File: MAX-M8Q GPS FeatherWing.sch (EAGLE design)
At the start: 28 parts, among them Q1 DMG3415U-7, Q2 2N2222, SW1 KMR2, X1 uFL

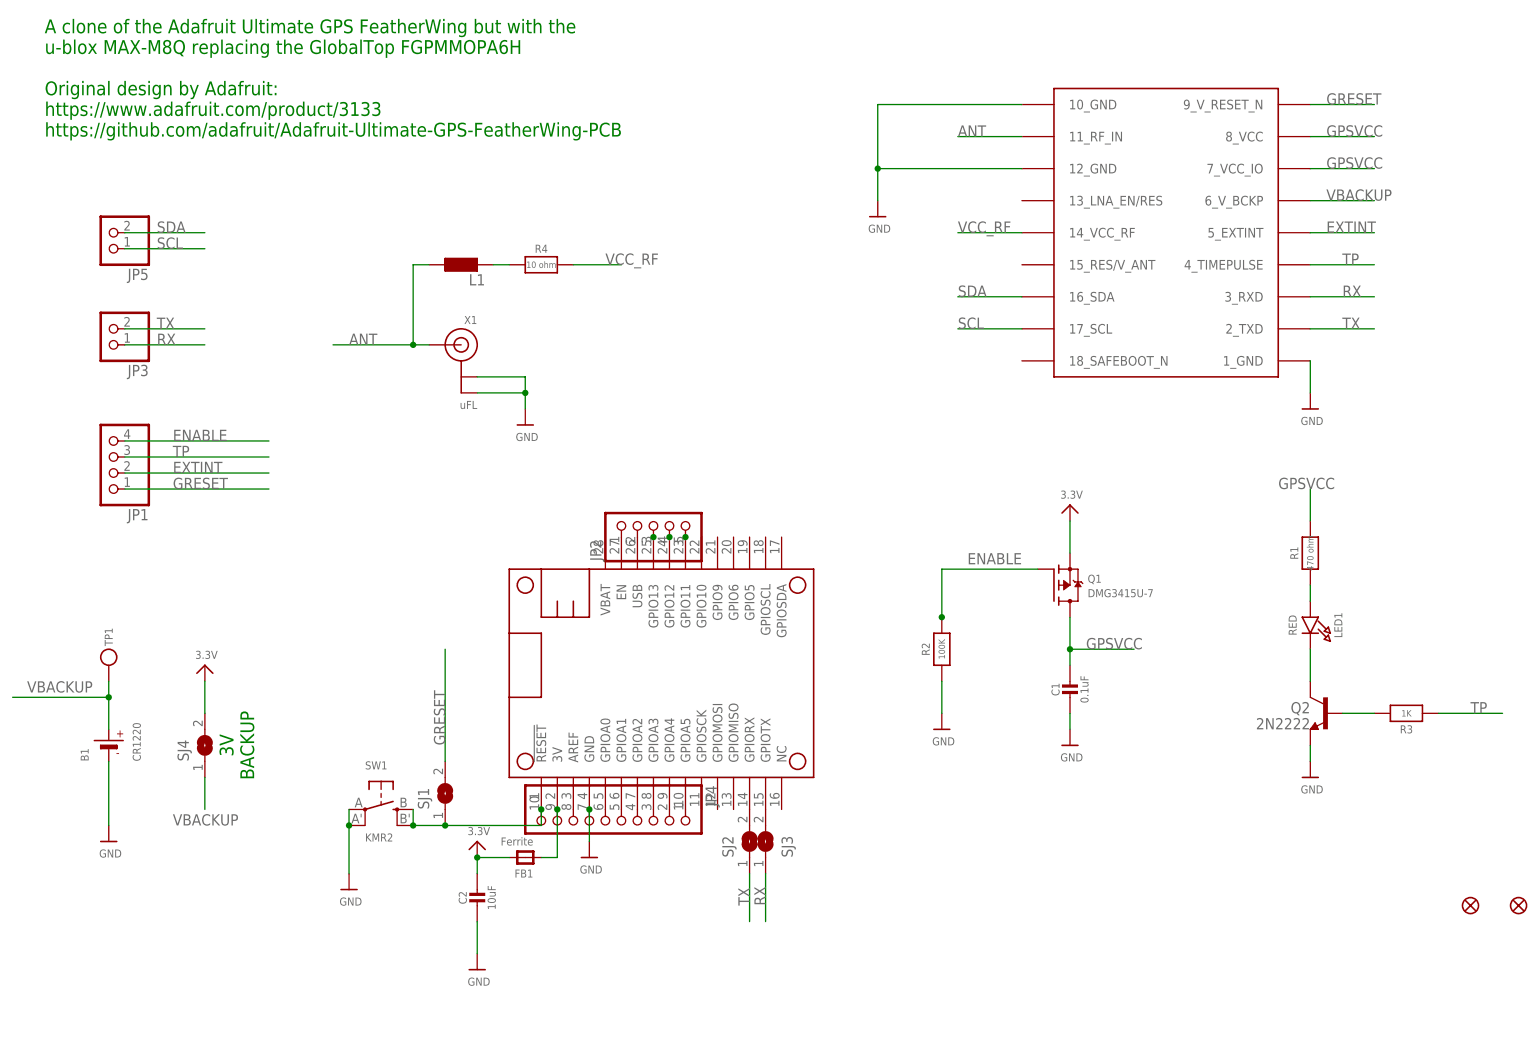
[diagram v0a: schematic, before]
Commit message: Minor tweaks. Included BOM.
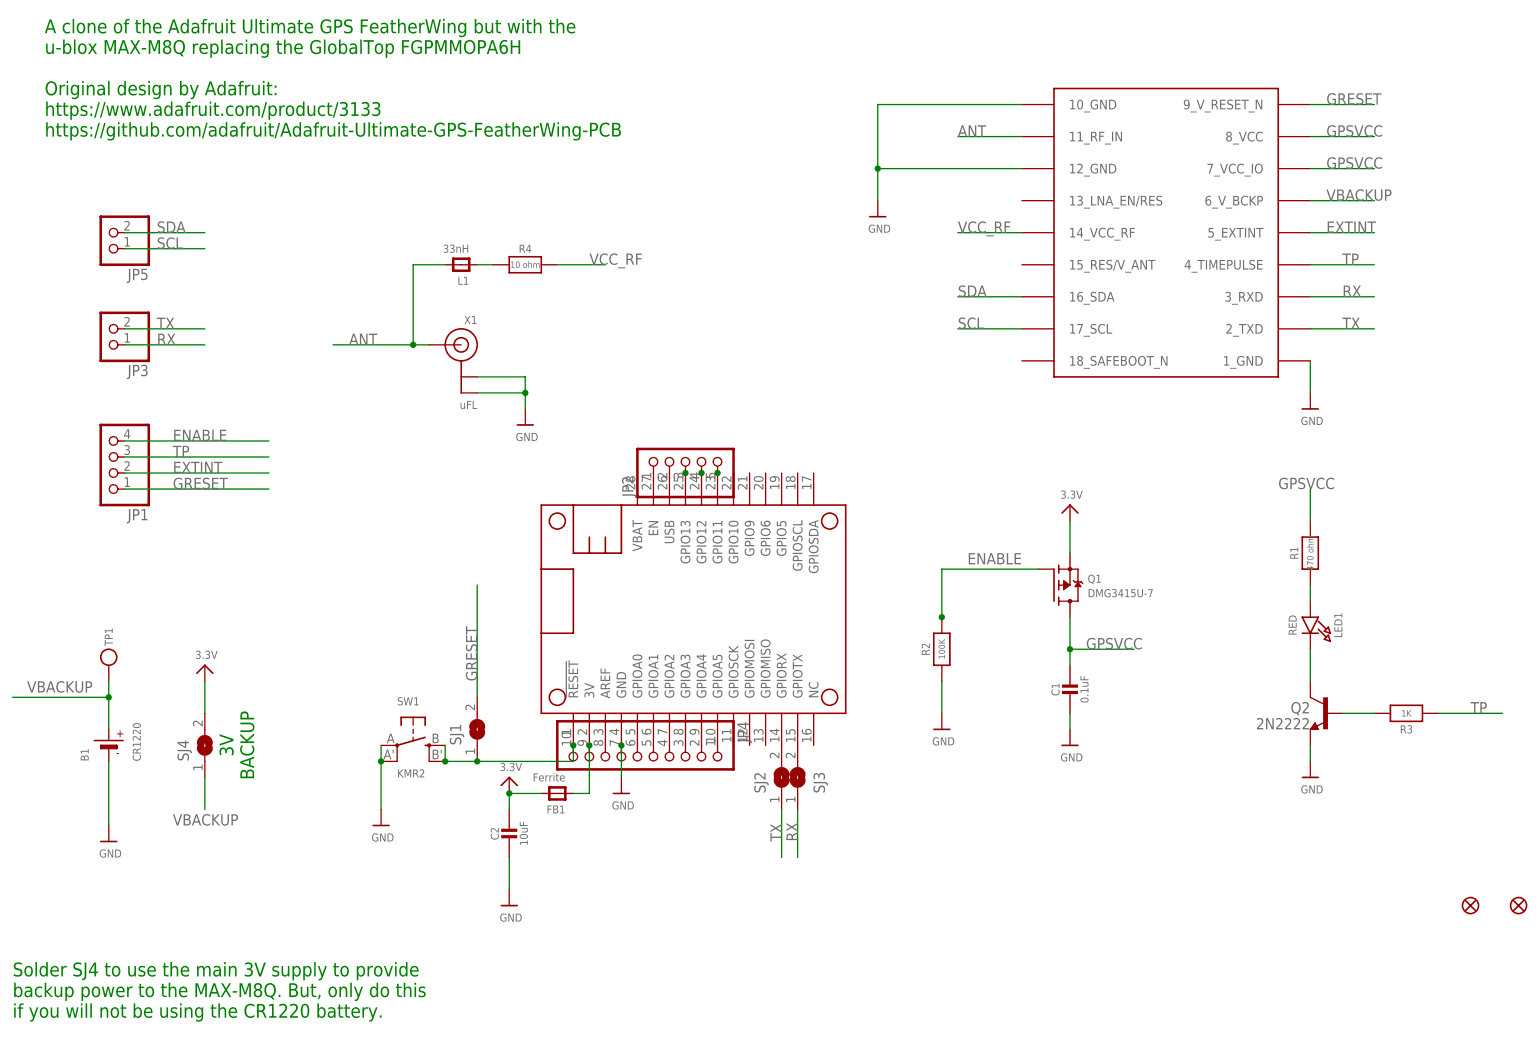
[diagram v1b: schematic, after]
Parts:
- L1: value (none) -> 33nH; device eagle-ltspice:LL2012C -> microbuilder:FERRITE-0805NO
- renumbered U$12 to U1
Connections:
- net ANT: now also L1.P$2; no longer L1.1
- net N$4: now also L1.P$1; no longer L1.2
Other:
- note added: "Solder SJ4 to use the main 3V supply to provide backup power to the MAX-M8Q. But, only do this if you will not be using the CR1220 battery."
- moved on the sheet: C2, FB1, JP2, JP4, R4, SJ1, SJ2, SJ3, SW1
